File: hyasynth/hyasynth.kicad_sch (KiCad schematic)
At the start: 38 parts, among them J1 Conn_01x04_Male, J2 Conn_01x02_Male, SW1 Power Switch, SW10 G# Ab, SW11 A, SW12 A# Bb, SW13 B, SW14 C, SW15 Down Octave, SW16 Function, SW17 Up Octave, SW18 Reset, SW2 Low C, SW3 C# Db, SW4 D, SW5 D# Eb, SW6 E, SW7 F, SW8 F# Gb, SW9 G, U1 EFM8LB12F64E-B-QFN32, U2 BH3544F

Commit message: Added GPIO and LED
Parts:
- added D?: WS2812B, LED_SMD:LED_WS2812B_PLCC4_5.0x5.0mm_P3.2mm, symbol LED:WS2812B
- added J?: Conn_01x08_Male, symbol Connector:Conn_01x08_Male
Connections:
- net GND: now also D?.3 (VSS), J?.8 (Pin_8)
- net VDD: now also D?.1 (VDD), J?.1 (Pin_1)
- new net GPIO_1: J?.5 (Pin_5)
- new net GPIO_2: J?.6 (Pin_6)
- new net GPIO_3: J?.7 (Pin_7)
- new net LED_Data: D?.4 (DIN)
- new net SPI_CLK: J?.3 (Pin_3)
- new net SPI_CS1: J?.2 (Pin_2)
- new net SPI_D: J?.4 (Pin_4)
- no-connect marks 2 -> 3
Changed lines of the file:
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@@
   (no_connect (at 224.79 105.41))
   (no_connect (at 224.79 100.33))
+  (no_connect (at 140.97 99.06))
   (polyline (pts (xy 176.53 135.89) (xy 176.53 198.12))
     (stroke (width 0) (type default) (color 0 0 0 0))
@@
     (stroke (width 0) (type default) (color 0 0 0 0))
   )
+  (wire (pts (xy 29.21 99.06) (xy 38.1 99.06))
+    (stroke (width 0) (type default) (color 0 0 0 0))
+  )
   (wire (pts (xy 44.45 31.75) (xy 44.45 33.02))
     (stroke (width 0) (type default) (color 0 0 0 0))
@@
     (stroke (width 0) (type default) (color 0 0 0 0))
   )
+  (wire (pts (xy 29.21 96.52) (xy 38.1 96.52))
+    (stroke (width 0) (type default) (color 0 0 0 0))
+  )
   (wire (pts (xy 208.28 59.69) (xy 208.28 60.96))
     (stroke (width 0) (type default) (color 0 0 0 0))
@@
     (stroke (width 0) (type default) (color 0 0 0 0))
   )
+  (wire (pts (xy 29.21 109.22) (xy 38.1 109.22))
+    (stroke (width 0) (type default) (color 0 0 0 0))
+  )
   (wire (pts (xy 187.96 97.79) (xy 175.26 97.79))
     (stroke (width 0) (type default) (color 0 0 0 0))
   )
+  (wire (pts (xy 29.21 104.14) (xy 38.1 104.14))
+    (stroke (width 0) (type default) (color 0 0 0 0))
+  )
   (wire (pts (xy 238.76 158.75) (xy 252.73 158.75))
     (stroke (width 0) (type default) (color 0 0 0 0))
@@
     (stroke (width 0) (type default) (color 0 0 0 0))
   )
+  (wire (pts (xy 29.21 106.68) (xy 38.1 106.68))
+    (stroke (width 0) (type default) (color 0 0 0 0))
+  )
   (wire (pts (xy 250.19 109.22) (xy 256.54 109.22))
     (stroke (width 0) (type default) (color 0 0 0 0))
@@
     (stroke (width 0) (type default) (color 0 0 0 0))
   )
+  (wire (pts (xy 114.3 99.06) (xy 125.73 99.06))
+    (stroke (width 0) (type default) (color 0 0 0 0))
+  )
   (wire (pts (xy 191.77 92.71) (xy 185.42 92.71))
     (stroke (width 0) (type default) (color 0 0 0 0))
@@
   )
   (wire (pts (xy 69.85 185.42) (xy 86.36 185.42))
+    (stroke (width 0) (type default) (color 0 0 0 0))
+  )
+  (wire (pts (xy 29.21 101.6) (xy 38.1 101.6))
     (stroke (width 0) (type default) (color 0 0 0 0))
   )
@@
     (effects (font (size 1.27 1.27)) (justify left bottom))
   )
+  (label "GPIO_3" (at 38.1 109.22 0)
+    (effects (font (size 1.27 1.27)) (justify left bottom))
+  )
   (label "Speaker_Out" (at 173.99 88.9 0)
     (effects (font (size 1.27 1.27)) (justify left bottom))
   )
+  (label "SPI_CLK" (at 38.1 99.06 0)
+    (effects (font (size 1.27 1.27)) (justify left bottom))
+  )
   (label "F" (at 80.01 175.26 0)
     (effects (font (size 1.27 1.27)) (justify left bottom))
@@
     (effects (font (size 1.27 1.27)) (justify left bottom))
   )
+  (label "SPI_D" (at 38.1 101.6 0)
+    (effects (font (size 1.27 1.27)) (justify left bottom))
+  )
   (label "Debug_Power" (at 100.33 34.29 0)
     (effects (font (size 1.27 1.27)) (justify left bottom))
@@
   )
   (label "C" (at 142.24 175.26 0)
+    (effects (font (size 1.27 1.27)) (justify left bottom))
+  )
+  (label "GPIO_1" (at 38.1 104.14 0)
     (effects (font (size 1.27 1.27)) (justify left bottom))
   )
@@
     (effects (font (size 1.27 1.27)) (justify right bottom))
   )
+  (label "SPI_CS1" (at 38.1 96.52 0)
+    (effects (font (size 1.27 1.27)) (justify left bottom))
+  )
   (label "DAC" (at 166.37 113.03 0)
     (effects (font (size 1.27 1.27)) (justify left bottom))
@@
   )
   (label "Up" (at 278.13 140.97 0)
+    (effects (font (size 1.27 1.27)) (justify left bottom))
+  )
+  (label "LED_Data" (at 114.3 99.06 0)
+    (effects (font (size 1.27 1.27)) (justify left bottom))
+  )
+  (label "GPIO_2" (at 38.1 106.68 0)
     (effects (font (size 1.27 1.27)) (justify left bottom))
   )
@@
     )
     (property "Datasheet" "" (id 3) (at 138.43 36.83 0)
+      (effects (font (size 1.27 1.27)) hide)
+    )
+    (pin "1")
+  )
+  (symbol (lib_id "power:VDD") (at 133.35 91.44 0) (unit 1)
+    (in_bom yes) (on_board yes) (fields_autoplaced)
+    (property "Reference" "#PWR?" (id 0) (at 133.35 95.25 0)
+      (effects (font (size 1.27 1.27)) hide)
+    )
+    (property "Value" "VDD" (id 1) (at 133.35 87.8355 0))
+    (property "Footprint" "" (id 2) (at 133.35 91.44 0)
+      (effects (font (size 1.27 1.27)) hide)
+    )
+    (property "Datasheet" "" (id 3) (at 133.35 91.44 0)
       (effects (font (size 1.27 1.27)) hide)
     )
@@
     (pin "1")
   )
+  (symbol (lib_id "power:GND") (at 133.35 106.68 0) (unit 1)
+    (in_bom yes) (on_board yes) (fields_autoplaced)
+    (property "Reference" "#PWR?" (id 0) (at 133.35 113.03 0)
+      (effects (font (size 1.27 1.27)) hide)
+    )
+    (property "Value" "GND" (id 1) (at 133.35 111.2425 0))
+    (property "Footprint" "" (id 2) (at 133.35 106.68 0)
+      (effects (font (size 1.27 1.27)) hide)
+    )
+    (property "Datasheet" "" (id 3) (at 133.35 106.68 0)
+      (effects (font (size 1.27 1.27)) hide)
+    )
+    (pin "1")
+  )
   (symbol (lib_id "Device:C_Polarized") (at 181.61 44.45 0) (unit 1)
     (in_bom yes) (on_board yes) (fields_autoplaced)
@@
     )
     (property "Datasheet" "" (id 3) (at 200.66 105.41 0)
+      (effects (font (size 1.27 1.27)) hide)
+    )
+    (pin "1")
+  )
+  (symbol (lib_id "power:GND") (at 29.21 111.76 0) (unit 1)
+    (in_bom yes) (on_board yes) (fields_autoplaced)
+    (property "Reference" "#PWR?" (id 0) (at 29.21 118.11 0)
+      (effects (font (size 1.27 1.27)) hide)
+    )
+    (property "Value" "GND" (id 1) (at 29.21 116.3225 0))
+    (property "Footprint" "" (id 2) (at 29.21 111.76 0)
+      (effects (font (size 1.27 1.27)) hide)
+    )
+    (property "Datasheet" "" (id 3) (at 29.21 111.76 0)
       (effects (font (size 1.27 1.27)) hide)
     )
@@
     )
     (pin "1")
+  )
+  (symbol (lib_id "Connector:Conn_01x08_Male") (at 24.13 101.6 0) (unit 1)
+    (in_bom yes) (on_board yes) (fields_autoplaced)
+    (property "Reference" "J?" (id 0) (at 24.765 89.9373 0))
+    (property "Value" "Conn_01x08_Male" (id 1) (at 24.765 92.7124 0))
+    (property "Footprint" "" (id 2) (at 24.13 101.6 0)
+      (effects (font (size 1.27 1.27)) hide)
+    )
+    (property "Datasheet" "~" (id 3) (at 24.13 101.6 0)
+      (effects (font (size 1.27 1.27)) hide)
+    )
+    (pin "1")
+    (pin "2")
+    (pin "3")
+    (pin "4")
+    (pin "5")
+    (pin "6")
+    (pin "7")
+    (pin "8")
   )
   (symbol (lib_id "power:GND") (at 208.28 50.8 0) (unit 1)
@@
     (pin "2")
   )
+  (symbol (lib_id "power:VDD") (at 29.21 93.98 0) (unit 1)
+    (in_bom yes) (on_board yes) (fields_autoplaced)
+    (property "Reference" "#PWR?" (id 0) (at 29.21 97.79 0)
+      (effects (font (size 1.27 1.27)) hide)
+    )
+    (property "Value" "VDD" (id 1) (at 29.21 90.3755 0))
+    (property "Footprint" "" (id 2) (at 29.21 93.98 0)
+      (effects (font (size 1.27 1.27)) hide)
+    )
+    (property "Datasheet" "" (id 3) (at 29.21 93.98 0)
+      (effects (font (size 1.27 1.27)) hide)
+    )
+    (pin "1")
+  )
+  (symbol (lib_id "LED:WS2812B") (at 133.35 99.06 0) (unit 1)
+    (in_bom yes) (on_board yes) (fields_autoplaced)
+    (property "Reference" "D?" (id 0) (at 143.6559 95.3348 0))
+    (property "Value" "WS2812B" (id 1) (at 143.6559 98.1099 0))
+    (property "Footprint" "LED_SMD:LED_WS2812B_PLCC4_5.0x5.0mm_P3.2mm" (id 2) (at 134.62 106.68 0)
+      (effects (font (size 1.27 1.27)) (justify left top) hide)
+    )
+    (property "Datasheet" "https://cdn-shop.adafruit.com/datasheets/WS2812B.pdf" (id 3) (at 135.89 108.585 0)
+      (effects (font (size 1.27 1.27)) (justify left top) hide)
+    )
+    (pin "1")
+    (pin "2")
+    (pin "3")
+    (pin "4")
+  )
   (symbol (lib_id "power:VDD") (at 123.19 29.21 0) (unit 1)
     (in_bom yes) (on_board yes) (fields_autoplaced)
@@
       (reference "#PWR0122") (unit 1) (value "VDD") (footprint "")
     )
+    (path "/1a008e7e-428d-4ec9-bd97-47c5036c95f6"
+      (reference "#PWR?") (unit 1) (value "VDD") (footprint "")
+    )
+    (path "/925eacfd-6eec-4ff3-9cb3-1e2927a6d3bd"
+      (reference "#PWR?") (unit 1) (value "GND") (footprint "")
+    )
+    (path "/9c7bd1ec-c05c-4ea6-a8bb-73abca5366be"
+      (reference "#PWR?") (unit 1) (value "GND") (footprint "")
+    )
+    (path "/cda66edb-6d48-4197-9a08-921e6c900e4a"
+      (reference "#PWR?") (unit 1) (value "VDD") (footprint "")
+    )
     (path "/1b998674-f60c-49d7-94e3-7408ec140148"
       (reference "BT1") (unit 1) (value "Battery_Cell") (footprint "Connector_PinSocket_2.54mm:PinSocket_1x02_P2.54mm_Vertical")
@@
       (reference "C9") (unit 1) (value "1u") (footprint "")
     )
+    (path "/d154ea11-c3c4-4175-94f0-50fe293d10f2"
+      (reference "D?") (unit 1) (value "WS2812B") (footprint "LED_SMD:LED_WS2812B_PLCC4_5.0x5.0mm_P3.2mm")
+    )
     (path "/748a6a47-fa8d-4129-923b-a3e1d8211e5e"
       (reference "J1") (unit 1) (value "Conn_01x04_Male") (footprint "Connector_PinSocket_2.54mm:PinSocket_1x04_P2.54mm_Vertical")
@@
       (reference "J2") (unit 1) (value "Conn_01x02_Male") (footprint "")
     )
+    (path "/c2386823-3fb5-4165-ab2c-17f69221afec"
+      (reference "J?") (unit 1) (value "Conn_01x08_Male") (footprint "")
+    )
     (path "/c8b9676b-221e-4cd7-863c-5d1cf75e0f5a"

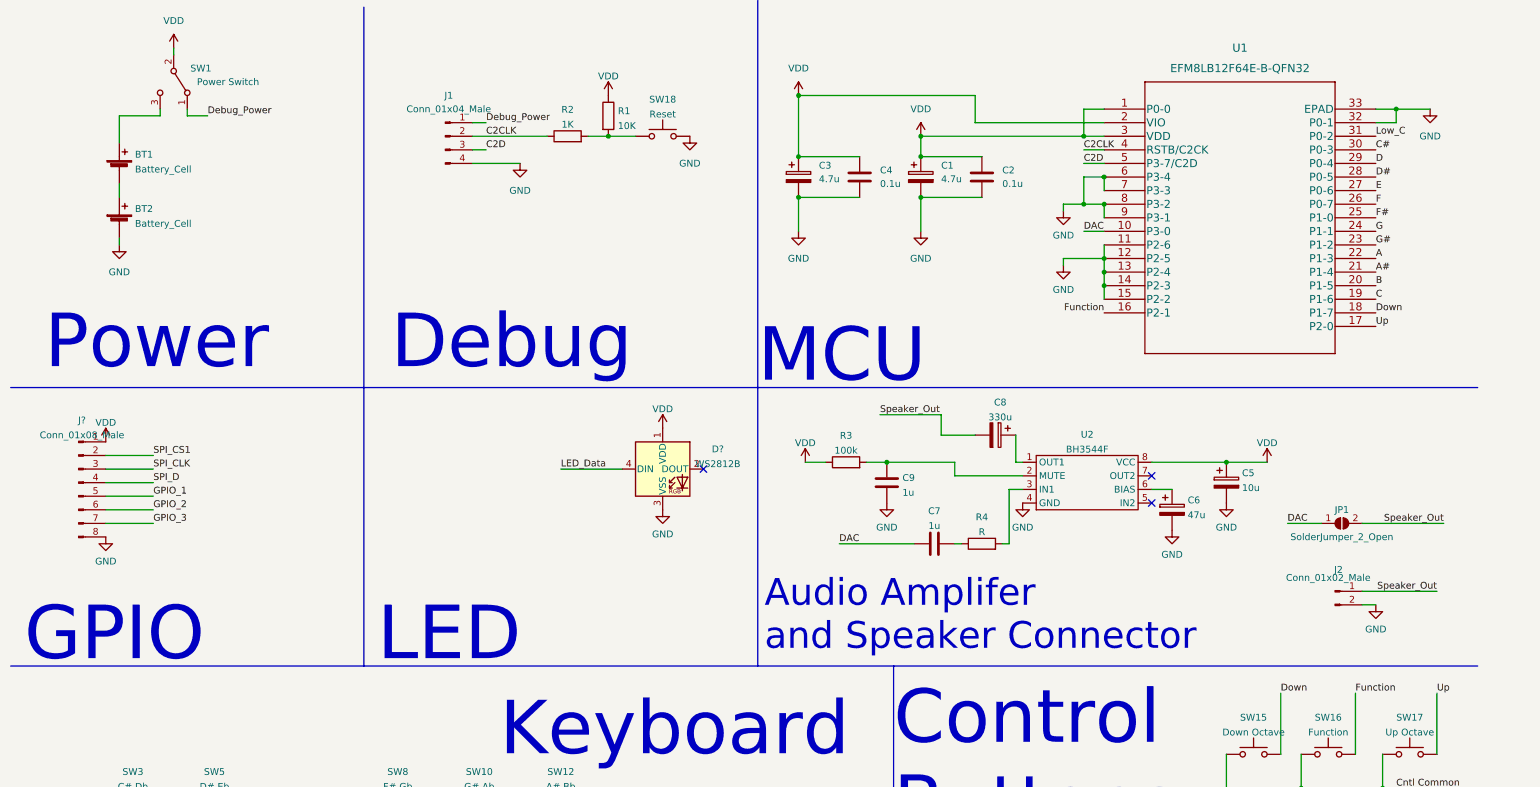
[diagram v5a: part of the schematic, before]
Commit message: Finished inital schematic design, added second amp, rearranged pins
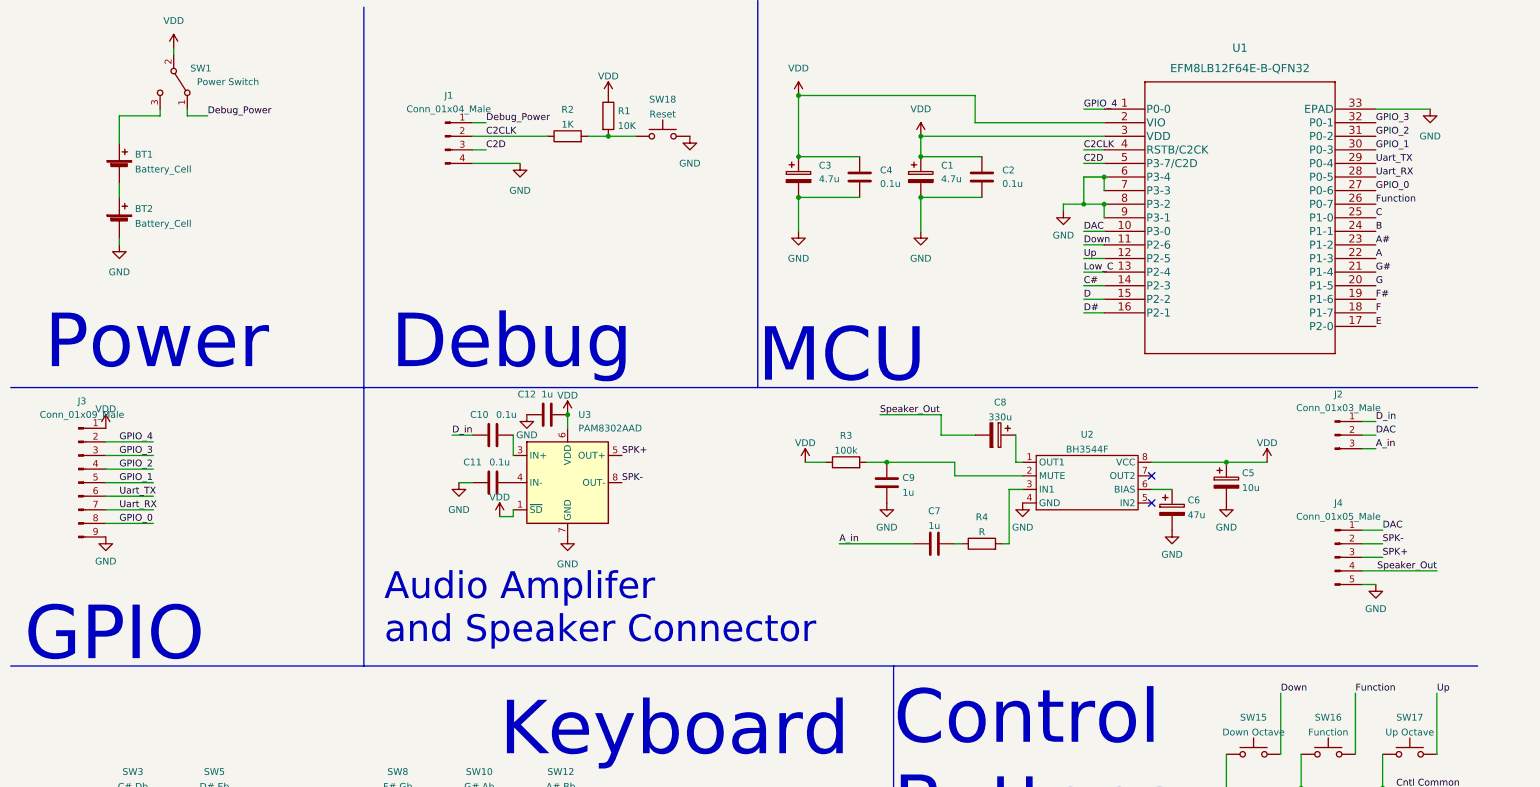
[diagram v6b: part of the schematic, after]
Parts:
- removed D?: WS2812B, LED_SMD:LED_WS2812B_PLCC4_5.0x5.0mm_P3.2mm, symbol LED:WS2812B
- removed J2: Conn_01x02_Male, symbol Connector:Conn_01x02_Male
- removed J?: Conn_01x08_Male, symbol Connector:Conn_01x08_Male
- removed JP1: SolderJumper_2_Open, symbol Jumper:SolderJumper_2_Open
- added C10, C11: 0.1u, symbol Device:C
- added C12: 1u, symbol Device:C
- added J2: Conn_01x03_Male, symbol Connector:Conn_01x03_Male
- added J3: Conn_01x09_Male, symbol Connector:Conn_01x09_Male
- added J4: Conn_01x05_Male, symbol Connector:Conn_01x05_Male
- added U3: PAM8302AAD, symbol Amplifier_Audio:PAM8302AAD
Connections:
- net A#: now also U1.23 (P1-2); no longer U1.21 (P1-4)
- net B: now also U1.24 (P1-1); no longer U1.20 (P1-5)
- net C: now also U1.25 (P1-0); no longer U1.19 (P1-6)
- net C#: now also U1.14 (P2-3); no longer U1.30 (P0-3)
- net D: now also U1.15 (P2-2); no longer U1.29 (P0-4)
- net D#: now also U1.16 (P2-1); no longer U1.28 (P0-5)
- net DAC: now also J2.2 (Pin_2), J4.1 (Pin_1); no longer C7.1
- net Down: now also U1.11 (P2-6); no longer U1.18 (P1-7)
- net E: now also U1.17 (P2-0); no longer U1.27 (P0-6)
- net F: now also U1.18 (P1-7); no longer U1.26 (P0-7)
- net F#: now also U1.19 (P1-6); no longer U1.25 (P1-0)
- net Function: now also U1.26 (P0-7); no longer U1.16 (P2-1)
- net G: now also U1.20 (P1-5); no longer U1.24 (P1-1)
- net G#: now also U1.21 (P1-4); no longer U1.23 (P1-2)
- net GND: now also C11.1, C12.1, J3.9 (Pin_9), J4.5 (Pin_5), U3.7 (GND); no longer U1.11 (P2-6), U1.12 (P2-5), U1.13 (P2-4), U1.14 (P2-3), U1.15 (P2-2), U1.32 (P0-1)
- net GPIO_1: now also U1.30 (P0-3), J3.5 (Pin_5)
- net GPIO_2: now also U1.31 (P0-2), J3.4 (Pin_4)
- net GPIO_3: now also U1.32 (P0-1), J3.3 (Pin_3)
- net Low_C: now also U1.13 (P2-4); no longer U1.31 (P0-2)
- net Speaker_Out: now also J4.4 (Pin_4)
- net Up: now also U1.12 (P2-5); no longer U1.17 (P2-0)
- net VDD: now also C12.2, J3.1 (Pin_1), U3.1 (~{SD}), U3.6 (VDD); no longer U1.1 (P0-0)
- new net: C10.2, U3.3 (IN+)
- new net: C11.2, U3.4 (IN-)
- new net A_in: C7.1, J2.3 (Pin_3)
- new net D_in: C10.1, J2.1 (Pin_1)
- new net GPIO_0: J3.8 (Pin_8), U1.27 (P0-6)
- new net GPIO_4: J3.2 (Pin_2), U1.1 (P0-0)
- new net SPK+: J4.3 (Pin_3), U3.5 (OUT+)
- new net SPK-: J4.2 (Pin_2), U3.8 (OUT-)
- new net Uart_RX: J3.7 (Pin_7), U1.28 (P0-5)
- new net Uart_TX: J3.6 (Pin_6), U1.29 (P0-4)
- no-connect marks 3 -> 2
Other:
- note removed: "LED"

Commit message: Footprint corrected
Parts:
- BT1, BT2: footprint Connector_PinSocket_2.54mm:PinSocket_1x02_P2.54mm_Vertical -> Battery:Battery AAA
- C1, C3: footprint (none) -> Capacitor_Tantalum_SMD:CP_EIA-6032-28_Kemet-C_Pad2.25x2.35mm_HandSolder
- C10, C11, C2, C4: footprint (none) -> Capacitor_SMD:C_0805_2012Metric_Pad1.18x1.45mm_HandSolder
- C12, C7, C9: footprint (none) -> Capacitor_Tantalum_SMD:CP_EIA-3528-21_Kemet-B_Pad1.50x2.35mm_HandSolder
- C5: footprint (none) -> Capacitor_Tantalum_SMD:CP_EIA-7343-31_Kemet-D_Pad2.25x2.55mm_HandSolder
- C6, C8: footprint (none) -> Capacitor_THT:CP_Radial_D8.0mm_P3.50mm
- J2, SW1: footprint (none) -> Connector_PinHeader_2.54mm:PinHeader_1x03_P2.54mm_Vertical
- J3: footprint (none) -> Connector_PinHeader_2.54mm:PinHeader_1x09_P2.54mm_Vertical
- J4: footprint (none) -> Connector_PinHeader_2.54mm:PinHeader_1x05_P2.54mm_Vertical
- R1, R2, R3, R4: footprint (none) -> Resistor_SMD:R_0805_2012Metric_Pad1.20x1.40mm_HandSolder
- U2: footprint (none) -> Package_SO:SOP-8_3.76x4.96mm_P1.27mm
- U3: footprint (none) -> Package_SO:MSOP-8_3x3mm_P0.65mm
